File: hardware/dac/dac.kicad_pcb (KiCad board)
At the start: 2 copper layers, 116.8 x 111.8 mm, 55 parts, among them IC1 EC1110120201_with_knurled_SHA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, J1 Conn_01x04, J2 Conn_02x08_Odd_Even, J3 Conn_02x08_Odd_Even, J4 Conn_02x08_Odd_Even, J5 Conn_01x02, J6 Conn_01x04, J7 Conn_01x04, Q1 Q_PNP_BCE, SW1 SW_SPST, SW2 SW_SPST, U1 74HC4040, U2 74LS08, U3 74LS174, U4 74HCT245, U5 74LS138, U6 DS1306, U7 IM6402, U8 MAX503, U9 MAX503, X1 4.9152MHz, Y1 32.768 kHz

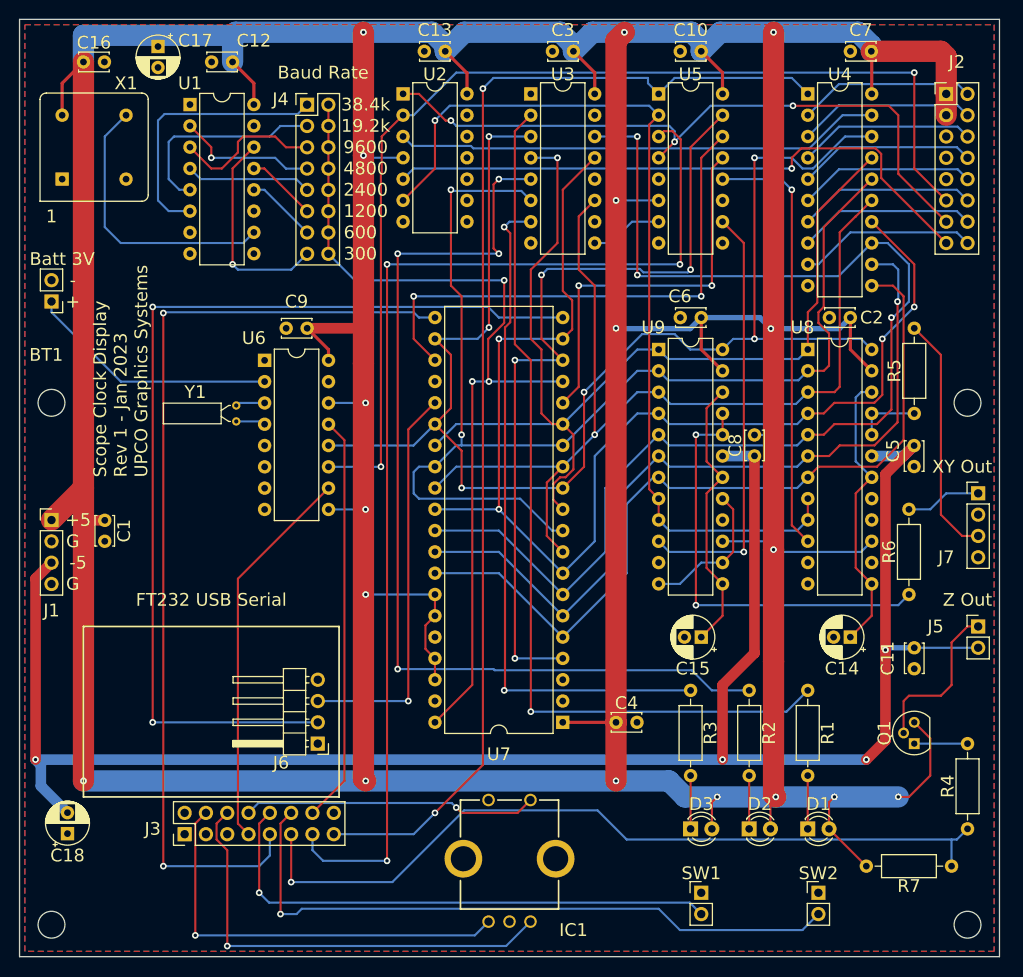
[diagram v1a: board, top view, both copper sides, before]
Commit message: working on Rev 2 DAC
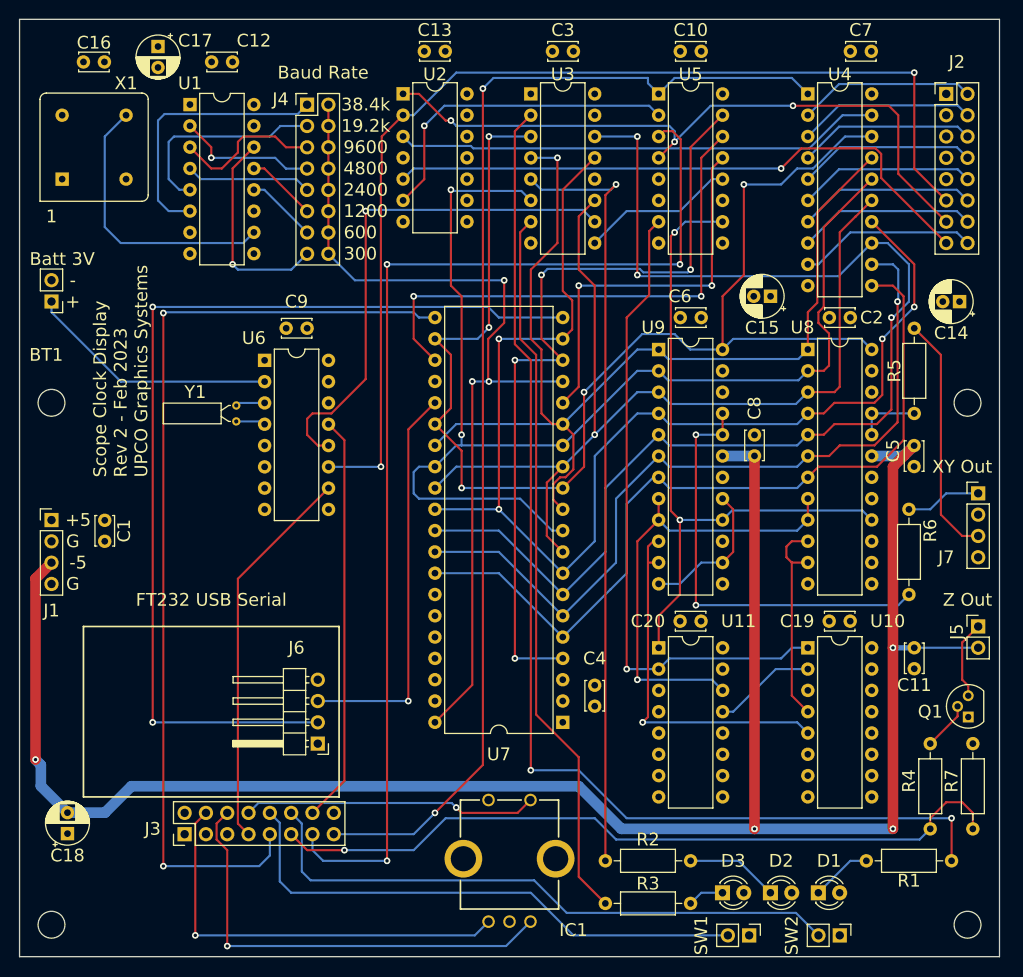
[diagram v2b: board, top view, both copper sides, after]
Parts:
- added C19: 0.1uF, Capacitor_THT:C_Disc_D3.4mm_W2.1mm_P2.50mm, F.Cu at (124.4, 132.7)
- added C20: 0.1uF, Capacitor_THT:C_Disc_D3.4mm_W2.1mm_P2.50mm, F.Cu at (106.7, 132.7)
- added U10: 74LS139, Package_DIP:DIP-16_W7.62mm, F.Cu at (119.4, 135.9)
- added U11: 74LS161, Package_DIP:DIP-16_W7.62mm, F.Cu at (101.6, 135.9)
- Q1: value Q_PNP_BCE -> 2N3906
- moved C14 42.1 mm to (137.5, 94.6)
- moved C15 41.5 mm to (114.9, 94.0)
- moved R3 27.4 mm to (95.2, 166.4), turned to 0 degrees
- moved R1 26.6 mm to (136.5, 161.3), turned to 180 degrees
- moved R2 26.6 mm to (95.2, 161.3), turned to 0 degrees
- moved D3 8.52 mm to (109.2, 165.1)
- moved D2 8.03 mm to (114.9, 165.1)
- moved D1 7.72 mm to (120.6, 165.1)
- moved SW1 7.65 mm to (112.4, 170.2), turned to -90 degrees
- moved Q1 7.18 mm to (138.5, 144.1)
- moved SW2 5.68 mm to (123.2, 170.2), turned to -90 degrees
- moved R7 5.12 mm to (139.1, 157.5), turned to 90 degrees
- moved R4 4.44 mm to (134.0, 157.5)
- moved C4 3.19 mm to (94.0, 142.9), turned to 90 degrees
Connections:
- C14 pad 1: Net-(C14-Pad1) -> +5V
- C15 pad 1: Net-(C15-Pad1) -> +5V
- Q1 pad 1: Net-(Q1-Pad1) -> +5V
- Q1 pad 2: Net-(J5-Pad1) -> Net-(Q1-Pad2)
- Q1 pad 3: +5V -> Net-(J5-Pad1)
- R4 pad 2: Net-(Q1-Pad1) -> Net-(Q1-Pad2)
- U3 pad 1: unconnected-(U3-Pad1) -> +5V
- U5 pad 12: /nDACX -> /nEXP
- U5 pad 7: /nEXP -> /nDACX
- U6 pad 12: /BD0 -> /LED3
- U8 pad 10: /nDACX -> /DAC_X_nWR
- U8 pad 11: GND -> /DAC_X_nWR
- U8 pad 13: Net-(C14-Pad1) -> +5V
- U8 pad 16: GND -> /nDACY
- U8 pad 18: Net-(C14-Pad1) -> +5V
- U8 pad 22: Net-(C14-Pad1) -> +5V
- U8 pad 8: /BA0 -> Net-(U8-Pad8)
- U8 pad 9: /BA0 -> Net-(U8-Pad8)
- U9 pad 10: /nDACY -> /DAC_Y_nWR
- U9 pad 11: GND -> /DAC_Y_nWR
- U9 pad 12: Net-(U9-Pad12) -> GND
- U9 pad 13: Net-(C15-Pad1) -> +5V
- U9 pad 14: Net-(U9-Pad12) -> GND
- U9 pad 16: GND -> /nDACY
- U9 pad 17: Net-(U9-Pad12) -> GND
- U9 pad 18: Net-(C15-Pad1) -> +5V
- U9 pad 22: Net-(C15-Pad1) -> +5V
- U9 pad 8: /BA0 -> Net-(U8-Pad8)
- U9 pad 9: /BA0 -> Net-(U8-Pad8)
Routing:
- net +5V: track 775.9 -> 0.00 mm, vias 18 -> 0
- net /BA0: track 109.5 -> 39.3 mm
- net /LED3: track 0.00 -> 61.9 mm, vias 0 -> 1
- net Net-(U8-Pad8): track 0.00 -> 54.7 mm, vias 0 -> 1
- net /DAC_Y_nWR: track 0.00 -> 44.2 mm, vias 0 -> 1
- net Net-(C14-Pad1): track 34.2 -> 0.00 mm
- net Net-(C15-Pad1): track 33.4 -> 0.00 mm
- net /LED0: track 106.8 -> 137.3 mm, vias 1 -> 2
- net /nDACY: track 51.1 -> 81.3 mm, vias 1 -> 2
- net /nDACX: track 51.5 -> 77.6 mm
- net /LED1: track 117.8 -> 92.1 mm, vias 4 -> 1
- net /DAC_X_nWR: track 0.00 -> 25.5 mm
- net Net-(U9-Pad12): track 17.3 -> 0.00 mm
- net -5V: track 229.4 -> 244.7 mm
- net GND: track 2.55 -> 17.3 mm
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- added copper zone on In2.Cu, net +5V
- added copper zone on In1.Cu, net GND
- removed copper zone on B.Cu, net GND
- removed copper zone on F.Cu, net GND
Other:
- copper layers 2 -> 4
- board text added: "Scope Clock Display Rev 2 - Feb 2023 UPCO Graphics Systems"
- board text removed: "Scope Clock Display Rev 1 - Jan 2023 UPCO Graphics Systems"

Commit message: software tweaks, working on case
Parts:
- removed IC1: EC1110120201_with_knurled_SHAFT, ShaftEnc:EC1110120201withknurledSHAFT
- added J8: Conn_01x02, Connector_PinHeader_2.54mm:PinHeader_1x02_P2.54mm_Vertical, F.Cu at (139.7, 153.7)
- added SW3: EN11-VSM1AF20, footprints:SWITCH_VSM1AF20_BIT, F.Cu at (81.3, 169.5)
- R1, R2, R3: value R_US -> 1.2k
- SW1, SW2: footprint Connector_PinHeader_2.54mm:PinHeader_1x02_P2.54mm_Vertical -> Button_Switch_THT:SW_Push_1P2T_Vertical_E-Switch_800UDP8P1A1M6
- moved SW1 61.8 mm to (50.8, 165.1)
- moved SW2 58.6 mm to (64.8, 165.1)
- moved R1 26.7 mm to (109.9, 161.3), turned to 0 degrees
- moved D1 6.75 mm to (125.7, 169.5)
- moved R7 6.35 mm to (134.0, 161.3), turned to 180 degrees
- moved D2 5.46 mm to (118.1, 169.5)
- moved D3 4.62 mm to (110.5, 169.5)
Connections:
- SW1 pad 2: /KD3 -> (no net)
- SW2 pad 2: /KD4 -> (no net)
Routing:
- net /LED4: track 0.00 -> 119.3 mm, vias 0 -> 2
- net /KD4: track 72.3 -> 11.3 mm
- net /KD3: track 64.8 -> 17.6 mm, vias 0 -> 1
- net /LED0: track 137.3 -> 110.6 mm
- net /KD2: track 35.2 -> 46.7 mm
- net /KD1: track 54.3 -> 43.2 mm
- net /KQ2: track 89.7 -> 84.0 mm
- net Net-(D2-K): track 11.1 -> 16.1 mm
- net Net-(D1-K): track 7.30 -> 10.6 mm
- net /KD0: track 50.8 -> 48.4 mm, vias 1 -> 2
- net Net-(D3-K): track 4.33 -> 6.39 mm
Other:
- board text added: "HV en"
- board text added: "Scope Clock Display Rev 2 - Dec 2023 UPCO Graphics Systems"
- board text removed: "Scope Clock Display Rev 2 - Feb 2023 UPCO Graphics Systems"
